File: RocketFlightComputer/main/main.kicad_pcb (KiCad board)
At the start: 4 copper layers, 53.7 x 53.7 mm, 128 parts, among them J1 BATT, Q2 SI2302, Q3 SI2302, Q4 SI2302, Y1 32.768kHz, Y2 24MHz, Y3 32.768kHz, Y4 32.768kHz

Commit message: Layout changes to incorporate power capacitors for the servos
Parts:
- C4: moved to F.Cu
- moved C4 3.98 mm to (116.8, 48.0), turned to 180 degrees
- moved 878-APS6404L-3SQR-SN1 3.46 mm to (121.8, 45.8)
- moved R33 3.20 mm to (123.6, 72.9)
- moved R9 1.82 mm to (125.5, 66.5)
- moved TP5 0.79 mm to (98.8, 64.5)
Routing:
- net +3.3V: track 94.0 -> 98.2 mm, vias 28 -> 29
- net Net-(MKL02Z32VFG4-PTB3/IRQ_10): track 31.6 -> 27.5 mm
- net /EMC_27: track 18.4 -> 14.3 mm
- net /EMC_28: track 18.4 -> 14.4 mm
- net /EMC_26: track 18.4 -> 14.3 mm
- net /EMC_24: track 18.4 -> 14.4 mm
- net /EMC_25: track 18.3 -> 14.3 mm
- net /EMC_29: track 18.3 -> 14.4 mm
- net Net-(MIMXRT1062DVL6B1-GPIO_EMC_08): track 13.7 -> 16.0 mm
- net /Pyro3_Test_39: track 34.3 -> 32.0 mm
- net GNDREF: track 272.2 -> 270.4 mm, vias 130 -> 129
- net Net-(MIMXRT1062DVL6B1-GPIO_B0_03): track 16.1 -> 14.9 mm
- net /3.3v_led: track 5.57 -> 4.55 mm
- net /M1M2: track 29.4 -> 28.5 mm
- net /BMP390_SDA1: track 66.3 -> 66.9 mm

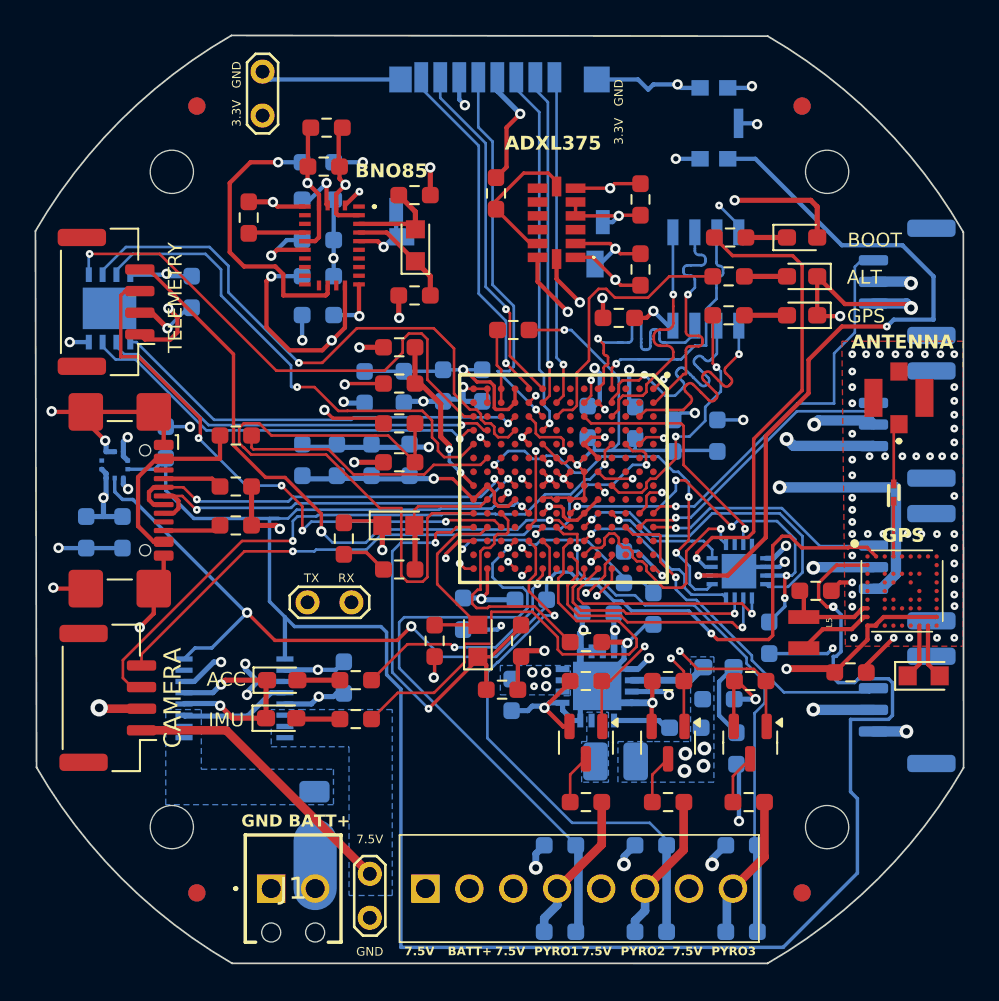
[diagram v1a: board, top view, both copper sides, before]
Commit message: Addition of all components in BOM, metal mounting plates, need to check psram if its ok for signals to pass under, all components need a double check
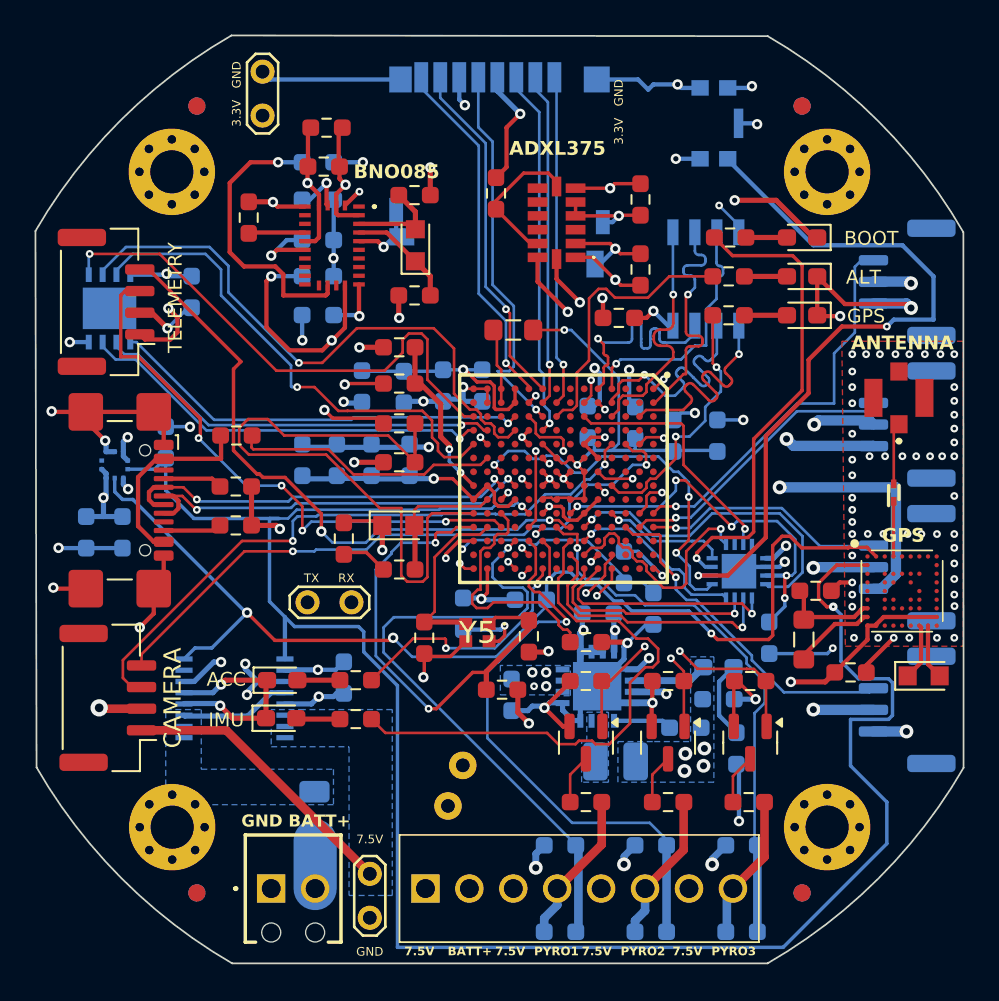
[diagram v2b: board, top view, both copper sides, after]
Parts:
- removed the L1 at (94.6, 54.8)
- removed the L3 at (102.1, 52.1)
- removed the REF** at (90.9, 77.5)
- removed the REF** at (128.8, 77.5)
- removed the REF** at (128.8, 39.6)
- removed the REF** at (90.9, 39.6)
- removed Y2: 24MHz, footprint:830050789
- added C41: 470uf, Capacitor_THT:C_Radial_D6.3mm_H11.0mm_P2.50mm, B.Cu at (106.9, 76.3)
- added FB1: 120, Resistor_SMD:R_0603_1608Metric_Pad0.98x0.95mm_HandSolder, F.Cu at (94.7, 54.8)
- added FB2: 120, Resistor_SMD:R_0603_1608Metric_Pad0.98x0.95mm_HandSolder, B.Cu at (101.9, 52.0)
- added REF**: MountingHole_2.5mm_Pad_Via, MountingHole:MountingHole_2.5mm_Pad_Via, F.Cu at (128.8, 77.5)
- added REF**: MountingHole_2.5mm_Pad_Via, MountingHole:MountingHole_2.5mm_Pad_Via, F.Cu at (90.9, 39.6)
- added REF**: MountingHole_2.5mm_Pad_Via, MountingHole:MountingHole_2.5mm_Pad_Via, F.Cu at (128.8, 39.6)
- added REF**: MountingHole_2.5mm_Pad_Via, MountingHole:MountingHole_2.5mm_Pad_Via, F.Cu at (91.0, 77.5)
- added Y5: XRCGB24M000F2P29R0, footprint:XRCGB, F.Cu at (108.6, 66.2)
- C10: renamed from C11; value 20pF -> 18pF
- C23, C24: value 12pF -> 10pF
- C38: value 4.7UF -> 4.7uF
- C39: value 0.1UF -> 0.1uF
- C9: renamed from C10; value 20pF -> 18pF
- D3: value GPS -> GPS LED
- L2: renamed from L4; footprint Resistor_SMD:R_0603_1608Metric_Pad0.98x0.95mm_HandSolder -> Inductor_SMD:L_0805_2012Metric_Pad1.05x1.20mm_HandSolder
- L3: renamed from L5; value 2.2μ -> 2.2μH; footprint ZOE-M8Q:0806 -> Inductor_SMD:L_0805_2012Metric_Pad1.05x1.20mm_HandSolder
- R11: renamed from R8; value 1k -> 470
- R12: renamed from R7; value 1k -> 470
- R5: renamed from R2; value 1k -> 470
- R9: renamed from R5; value 1k -> 470
- moved C23 0.62 mm to (105.5, 66.5), turned to -90 degrees
- moved C24 0.52 mm to (111.6, 66.5)
- renumbered 878-APS6404L-3SQR-SN1 to APS6404L-SQH-SN1, BMP390 to BMP1, BNO85 to BNO085, C12 to C11, C13 to C12, C14 to C13, C15 to C14, C16 to C15, C17 to C16, C18 to C17, C19 to C18, C6 to C19, C37 to C30, C30 to C31, C31 to C32, C32 to C33, C33 to C34, C34 to C35, C35 to C36, C36 to C37, C7 to C6, C8 to C7, C9 to C8, D8 to D1, D1 to D2, D6 to D5, D2 to D6, D5 to D7, F2 to F1, FID4 to FID2, FID2 to FID3, FID5 to FID4, FID3 to FID5, L2 to L1, MKL02Z32VFG4 to MKL02Z32VFG1, Q2 to Q1, Q3 to Q2, Q4 to Q3, Resistor3 to R1, R4 to R10, R9 to R13, R15 to R14, R16 to R15, R17 to R16, R10 to R17, R12 to R18, R14 to R19, Resistor4 to R2, R18 to R20, R19 to R21, R20 to R22, R21 to R23, R23 to R24, R24 to R25, R27 to R26, R28 to R27, R29 to R28, R30 to R29, R1 to R3, R31 to R30, R32 to R31, R33 to R4, R34 to R6, R3 to R7, R11 to R8, J1 to ScrewTerminal2, TP5 to TP2, TP2 to TP3, U-BLOX_ZOE_M8Q-0-10 to U-BLOX_ZOE_M8Q-0-1
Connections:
- C23 pad 1: GNDREF -> /N11
- C23 pad 2: /N11 -> GNDREF
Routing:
- net +7.5V: track 122.4 -> 127.5 mm
- net GNDREF: track 270.4 -> 274.7 mm, vias 129 -> 130
- net /P11: track 25.1 -> 29.1 mm
- net /Pyro2_Test_41: track 32.5 -> 33.8 mm
- net Net-(MIMXRT1062DVL6B1-GPIO_AD_B1_14): track 30.9 -> 32.2 mm
- net +3.3V: track 98.2 -> 97.0 mm
- net /Pyro1_Test_40: track 35.9 -> 37.0 mm
- net /N11: track 11.1 -> 10.2 mm
- net /BMP390_SCL1: track 115.7 -> 115.0 mm
- net Net-(MIMXRT1062DVL6B1-VDD_SNVS_CAP): track 13.5 -> 14.2 mm
- net Net-(MIMXRT1062DVL6B1-GPIO_AD_B1_15): track 13.8 -> 14.4 mm
- net /BMP390_SDA1: track 66.9 -> 66.4 mm
- net /Xbee_RX: track 35.8 -> 36.4 mm

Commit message: Last commit before changing bga to trace clearance of 6mils
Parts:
- moved TP1 3.61 mm to (99.3, 34.5), turned to 180 degrees
- moved C25 0.45 mm to (115.4, 53.8)
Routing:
- net GNDREF: track 274.7 -> 260.8 mm, vias 130 -> 132
- net /D1: track 23.8 -> 34.2 mm
- net Net-(KMR241GLFS1-COM_1): track 42.3 -> 32.0 mm
- net /D2: track 24.1 -> 34.3 mm
- net /CS: track 24.5 -> 34.1 mm
- net /D3: track 28.9 -> 34.3 mm
- net Net-(MIMXRT1062DVL6B1-GPIO_EMC_08): track 16.0 -> 19.7 mm
- net /D0: track 30.9 -> 34.3 mm
- net /Pyro2_Test_41: track 33.8 -> 36.7 mm
- net +BATT: track 6.42 -> 5.15 mm
- net /Servo2_PWM: track 14.2 -> 15.4 mm
- net /Servo4_PWM: track 22.7 -> 21.5 mm
- net /SD_B0_01: track 22.3 -> 21.2 mm
- net /BMP390_SDA1: track 66.4 -> 65.2 mm
- net /BMP390_SCL1: track 115.0 -> 114.2 mm
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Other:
- board text added: "GND 3.3V"
- board text removed: "3.3V GND"

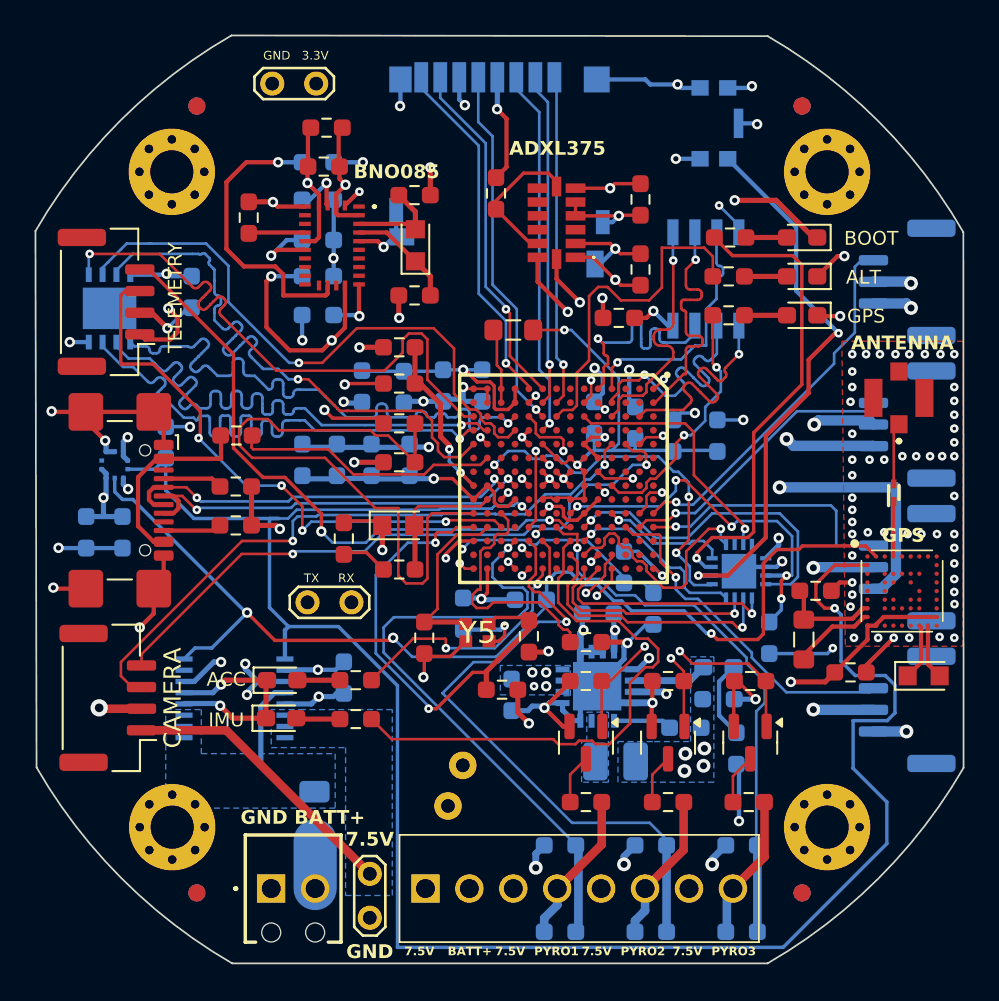
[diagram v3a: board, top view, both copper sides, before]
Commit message: First commit with 0.1mm traces and 02mm by 0.43mm vias to fit pcbway standard manufacturing + corrections of PR'S like uart RX of component to TX of mcu
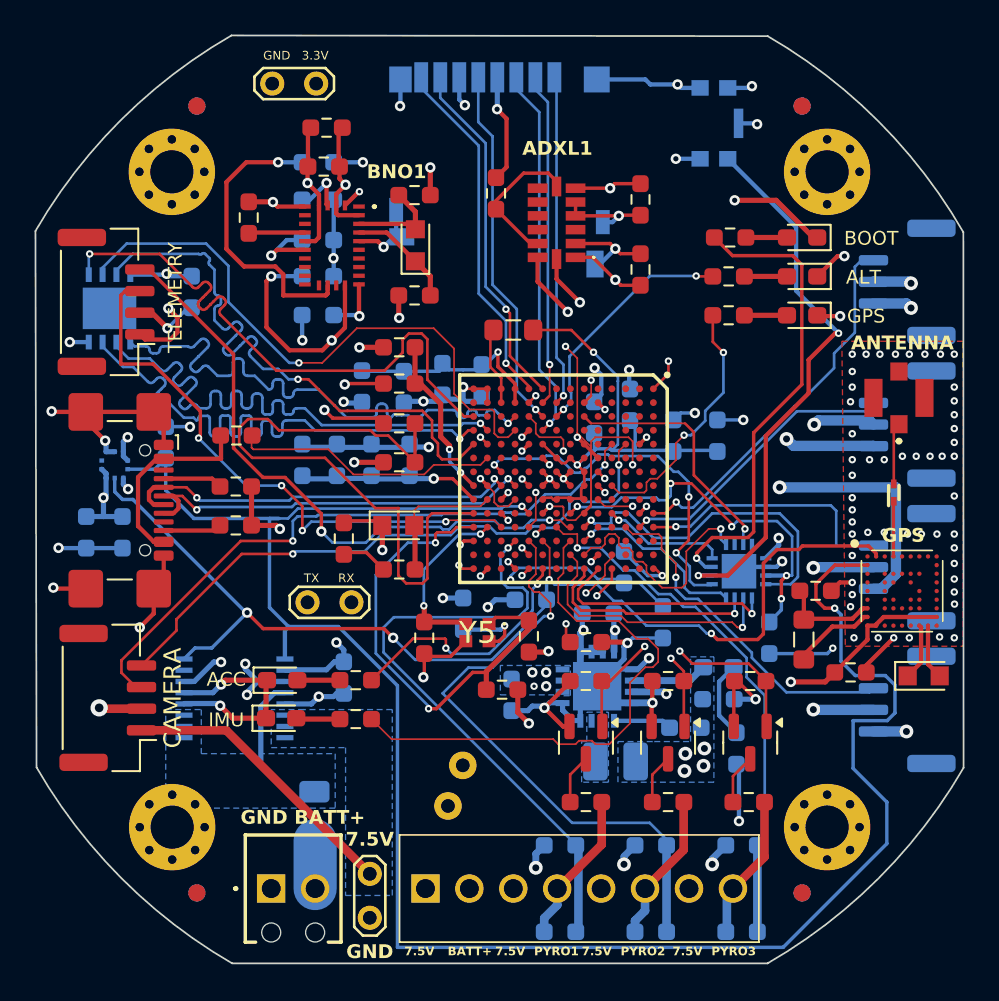
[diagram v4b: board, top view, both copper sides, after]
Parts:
- removed APS6404L-SQH-SN1: PSRAM, footprint:APS6404L
- removed C4: 0.22uF, Resistor_SMD:R_0603_1608Metric_Pad0.98x0.95mm_HandSolder
- moved C26 1.08 mm to (117.4, 53.1)
- moved C12 0.96 mm to (119.3, 65.6)
- moved C14 0.38 mm to (106.6, 51.6)
- moved C18 0.30 mm to (108.9, 51.7)
- renumbered ADXL375 to ADXL1, BNO085 to BNO1, INA260 to INA1
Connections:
- net /BMO085_SCL renamed /BNO085_SCL
- net /BMO085_SDA renamed /BNO085_SDA
- MIMXRT1062DVL6B1 pad A2: /EMC_27 -> unconnected-(MIMXRT1062DVL6B1-GPIO_EMC_27-PadA2)
- MIMXRT1062DVL6B1 pad B3: /EMC_26 -> unconnected-(MIMXRT1062DVL6B1-GPIO_EMC_26-PadB3)
- MIMXRT1062DVL6B1 pad D1: /EMC_28 -> unconnected-(MIMXRT1062DVL6B1-GPIO_EMC_28-PadD1)
- MIMXRT1062DVL6B1 pad D13: /Reserve_TX -> /Reserve_RX
- MIMXRT1062DVL6B1 pad D14: /Reserve_RX -> /Reserve_TX
- MIMXRT1062DVL6B1 pad D2: /EMC_25 -> unconnected-(MIMXRT1062DVL6B1-GPIO_EMC_25-PadD2)
- MIMXRT1062DVL6B1 pad D3: /EMC_24 -> unconnected-(MIMXRT1062DVL6B1-GPIO_EMC_24-PadD3)
- MIMXRT1062DVL6B1 pad E1: /EMC_29 -> unconnected-(MIMXRT1062DVL6B1-GPIO_EMC_29-PadE1)
- MIMXRT1062DVL6B1 pad G11: /Xbee_RX -> /Xbee_TX
- MIMXRT1062DVL6B1 pad M11: /Xbee_TX -> /Xbee_RX
- S4B-PH-K-S_LF__SN_1 pad 3: /Xbee_TX -> /Xbee_RX
- S4B-PH-K-S_LF__SN_1 pad 4: /Xbee_RX -> /Xbee_TX
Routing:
- net +3.3V: track 96.4 -> 111.2 mm, vias 29 -> 34
- net /EMC_29: track 14.4 -> 0.00 mm, vias 1 -> 0
- net /EMC_28: track 14.4 -> 0.00 mm, vias 1 -> 0
- net /EMC_24: track 14.4 -> 0.00 mm, vias 1 -> 0
- net /EMC_27: track 14.4 -> 0.00 mm, vias 1 -> 0
- net /EMC_25: track 14.3 -> 0.00 mm, vias 1 -> 0
- net /EMC_26: track 14.3 -> 0.00 mm, vias 1 -> 0
- net GNDREF: track 260.8 -> 255.0 mm, vias 132 -> 131
- net Net-(MIMXRT1062DVL6B1-GPIO_EMC_08): track 19.7 -> 14.1 mm, vias 0 -> 2
- net /Xbee_TX: track 33.4 -> 36.4 mm, vias 4 -> 2
- net /ADXL375_SDA2: track 21.7 -> 24.7 mm
- net /Xbee_RX: track 35.9 -> 33.4 mm, vias 2 -> 4
- net Net-(MIMXRT1062DVL6B1-VDD_USB_CAP): track 19.3 -> 17.6 mm
- net /Pyro2_Test_41: track 36.7 -> 35.2 mm
- net Net-(MIMXRT1062DVL6B1-VDD_SNVS_CAP): track 14.2 -> 15.7 mm, vias 0 -> 2
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
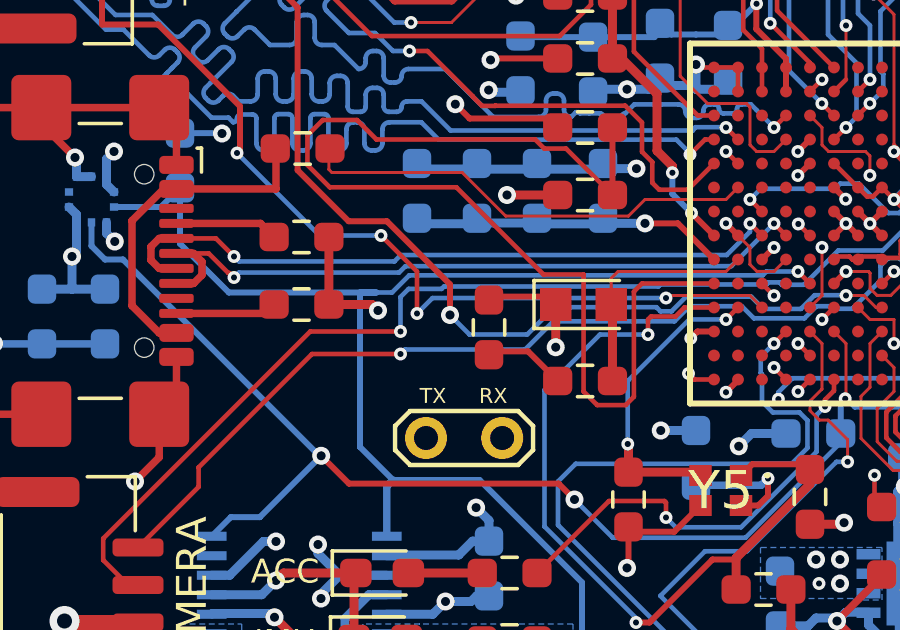
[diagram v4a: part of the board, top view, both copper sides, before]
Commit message: Switch to KICAD10 and correction of TX RX
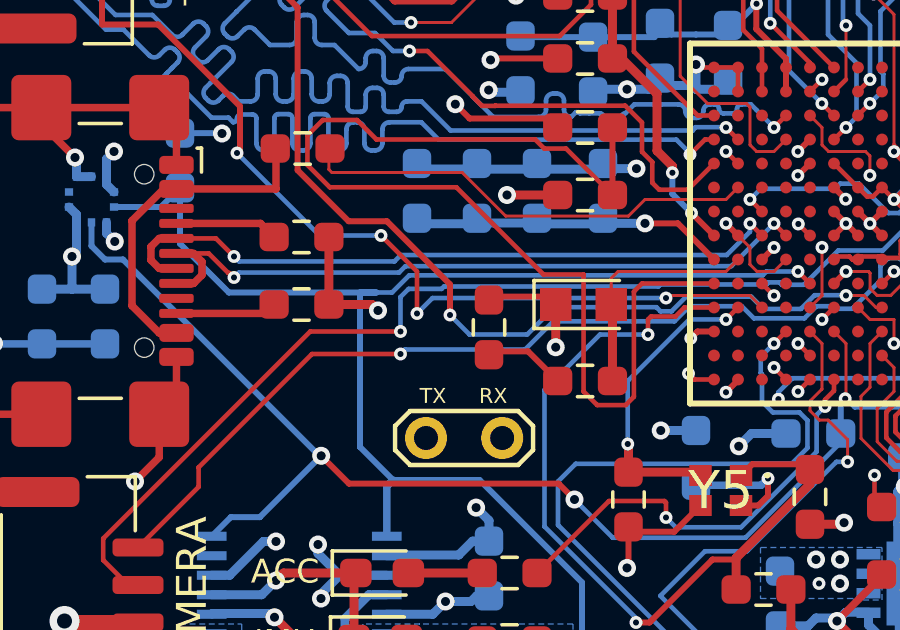
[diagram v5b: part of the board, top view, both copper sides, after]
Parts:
- C40: value 1uF -> 0.1uF
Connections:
- MIMXRT1062DVL6B1 pad C5: /Cam_TX -> /Cam_RX
- MIMXRT1062DVL6B1 pad D5: /Cam_RX -> /Cam_TX
- MIMXRT1062DVL6B1 pad G11: /Xbee_TX -> /Xbee_RX
- MIMXRT1062DVL6B1 pad M11: /Xbee_RX -> /Xbee_TX
- S4B-PH-K-S_LF__SN_1 pad 3: /Xbee_RX -> /Xbee_TX
- S4B-PH-K-S_LF__SN_1 pad 4: /Xbee_TX -> /Xbee_RX
- S4B-PH-K-S_LF__SN_2 pad 3: /Cam_RX -> /Cam_TX
- S4B-PH-K-S_LF__SN_2 pad 4: /Cam_TX -> /Cam_RX
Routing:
- net /Xbee_TX: track 36.4 -> 33.4 mm, vias 2 -> 4
- net /Xbee_RX: track 33.4 -> 36.4 mm, vias 4 -> 2
- net /Cam_TX: track 35.9 -> 37.5 mm
- net /Cam_RX: track 37.5 -> 35.9 mm
